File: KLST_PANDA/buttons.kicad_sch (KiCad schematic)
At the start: 0 parts

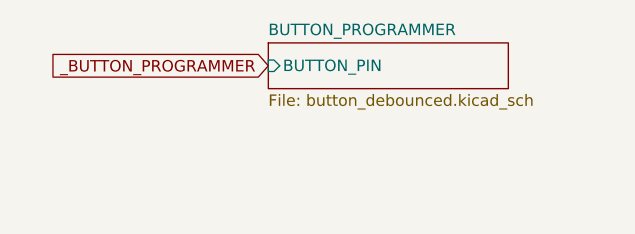
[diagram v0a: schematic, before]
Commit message: updated pin names, configured all pins and most peripherals,
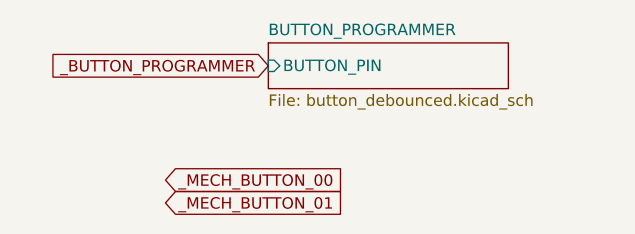
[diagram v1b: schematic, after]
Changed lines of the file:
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@@
 (kicad_sch (version 20230121) (generator eeschema)
   (paper "A4")
+  (global_label "_MECH_BUTTON_00" (shape input) (at 143.51 113.03 0) (fields_autoplaced)
+    (effects (font (size 1.27 1.27)) (justify left))
+    (property "Intersheetrefs" "${INTERSHEET_REFS}" (at 164.1352 113.03 0)
+      (effects (font (size 1.27 1.27)) (justify left) hide)
+    )
+  )
+  (global_label "_MECH_BUTTON_01" (shape input) (at 143.51 115.57 0) (fields_autoplaced)
+    (effects (font (size 1.27 1.27)) (justify left))
+    (property "Intersheetrefs" "${INTERSHEET_REFS}" (at 164.1352 115.57 0)
+      (effects (font (size 1.27 1.27)) (justify left) hide)
+    )
+  )
   (global_label "_BUTTON_PROGRAMMER" (shape input) (at 154.94 100.33 180) (fields_autoplaced)
     (effects (font (size 1.27 1.27)) (justify right))
